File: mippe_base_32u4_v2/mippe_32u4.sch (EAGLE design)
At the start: 29 parts, among them J2 USB, J5 BURNIN, SW1 BTN-PTS810, U1 ATMEGA32U4-XUMU, Y1 16MHz

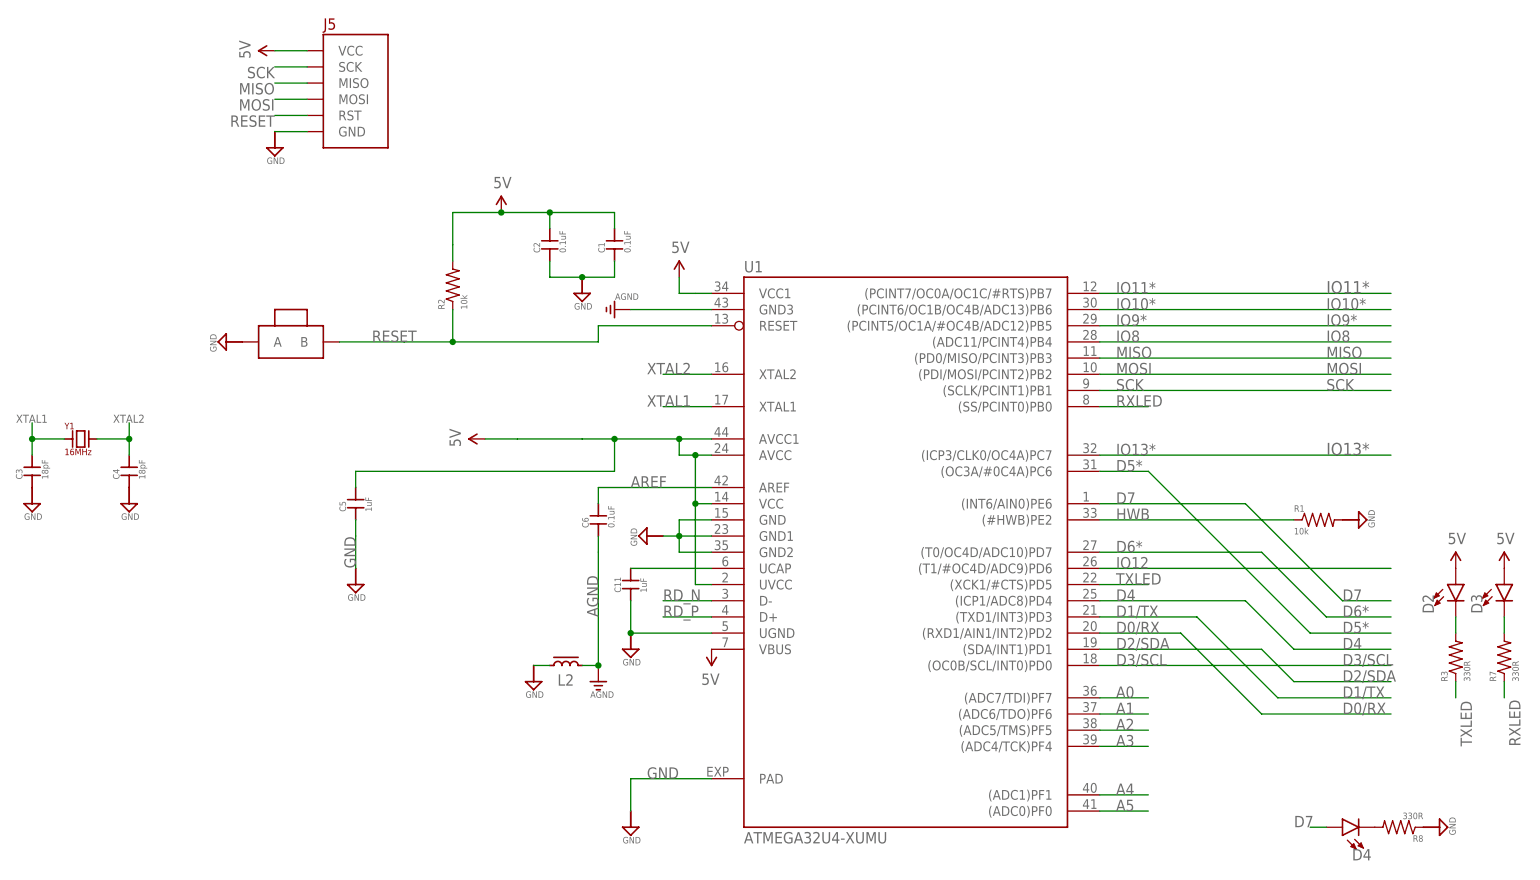
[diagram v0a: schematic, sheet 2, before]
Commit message: 32u4 0402 rev
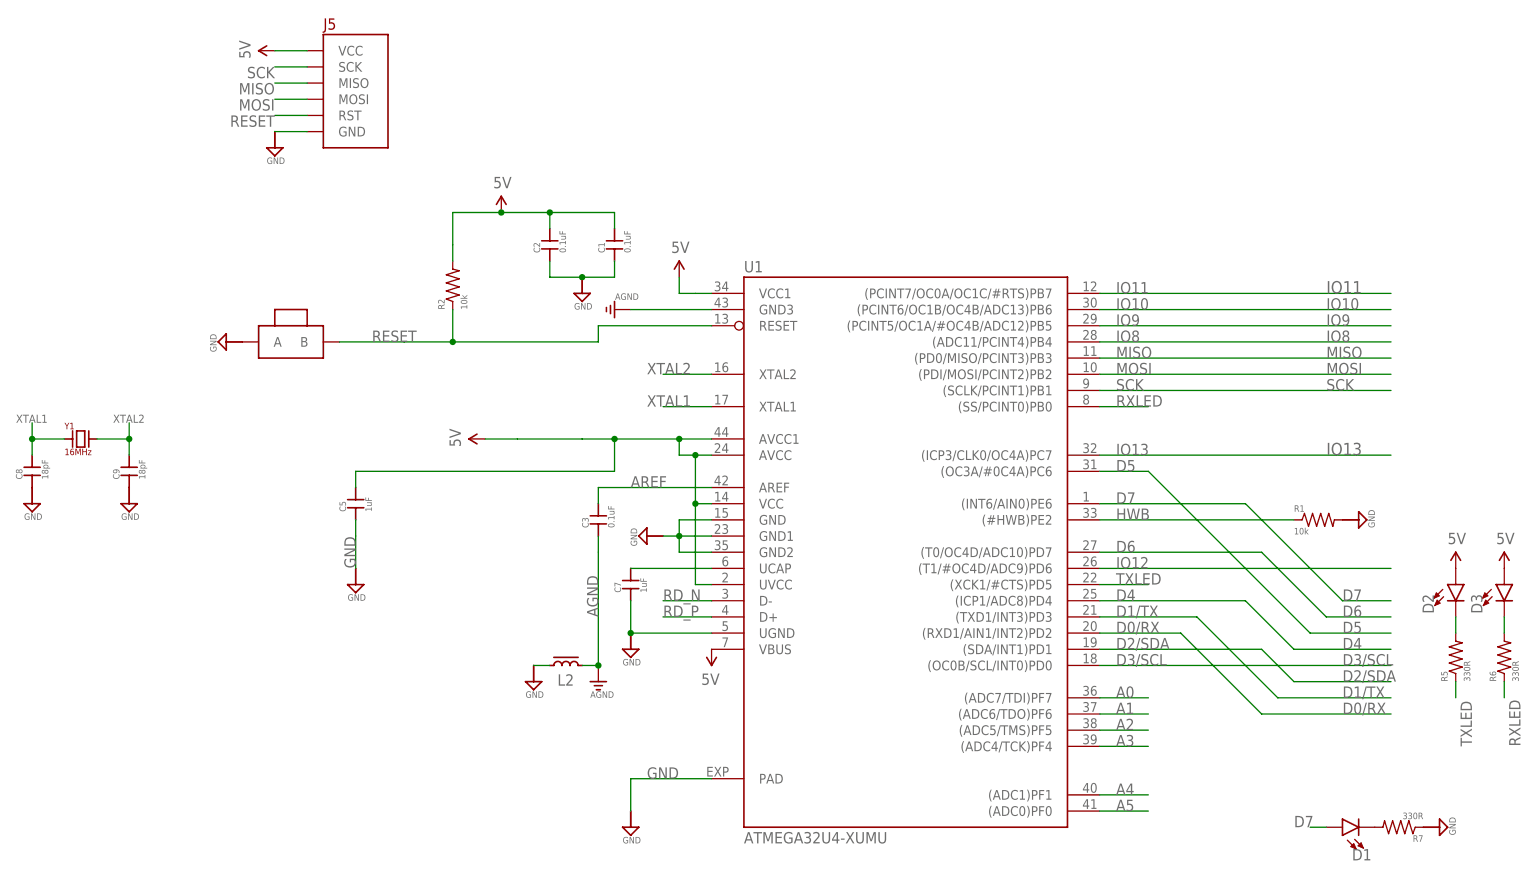
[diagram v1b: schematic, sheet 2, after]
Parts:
- removed C10: 1uF, scono:CAP0402-CAP
- removed R8: 330R, scono:R-US_R0402
- added C8: 18pF, scono:CAP0402-CAP
- added R6: 330R, scono:R-US_R0402
- C3, C4: value 18pF -> 0.1uF
- C6: value 0.1uF -> 1uF
- C9: value 0.1uF -> 18pF
- R3: value 330R -> 22R
- R5: value 22R -> 330R
- renumbered C11 to C7, D4 to D1
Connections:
- net D5* renamed D5
- net D6* renamed D6
- net IO10* renamed IO10
- net IO11* renamed IO11
- net IO13* renamed IO13
- net IO9* renamed IO9
- net 5V: now also C4.2, C6.2; no longer C10.2, C9.2
- net AGND: now also C3.1; no longer C6.1
- net AREF: now also C3.2; no longer C6.2
- net D_P: now also R3.1; no longer R5.1
- net GND: now also C6.1, C8.1, R7.1; no longer C10.1, C3.1, R8.1
- net N$1: now also R5.2; no longer R3.2
- net N$2: now also R6.2; no longer R7.2
- net N$4: now also R7.2; no longer R8.2
- net RD_P: now also R3.2; no longer R5.2
- net RXLED: now also R6.1; no longer R7.1
- net TXLED: now also R5.1; no longer R3.1
- net XTAL1: now also C8.2; no longer C3.2
- net XTAL2: now also C9.2; no longer C4.2
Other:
- moved on the sheet: C3, R7
